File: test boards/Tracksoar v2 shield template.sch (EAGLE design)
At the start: 3 parts

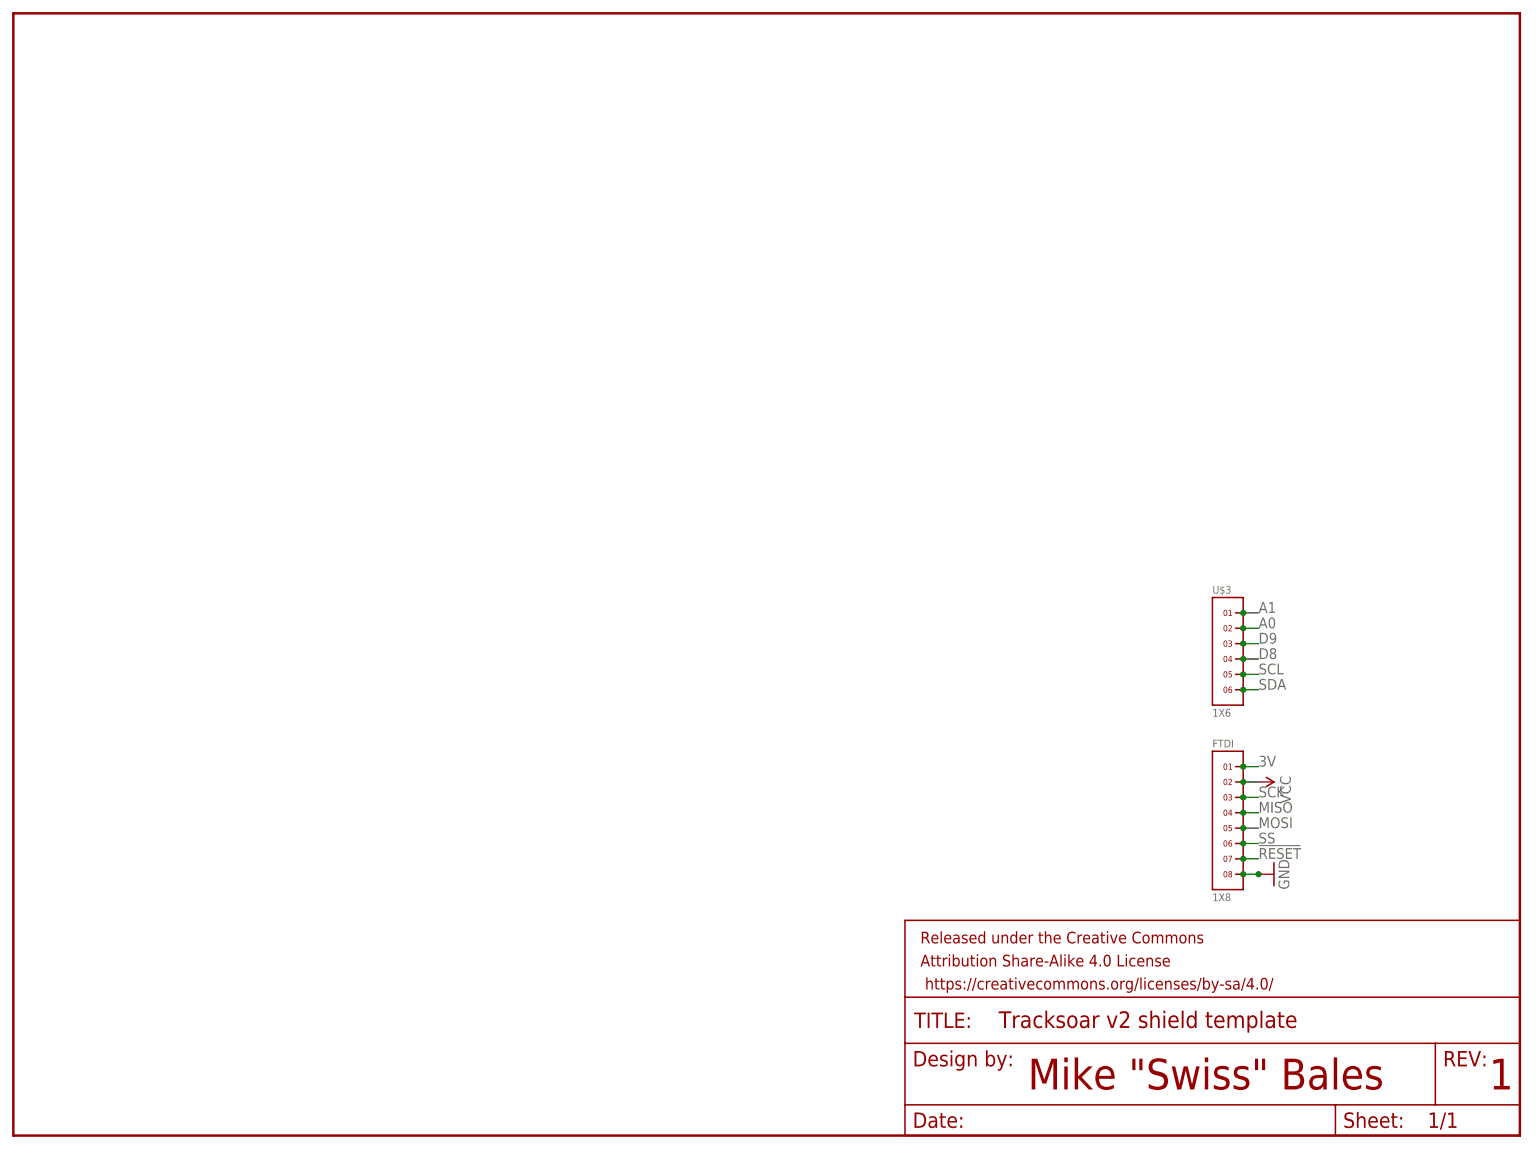
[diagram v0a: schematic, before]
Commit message: updated shield template
updated shield template to be a breakout board for all IO into .1" headers
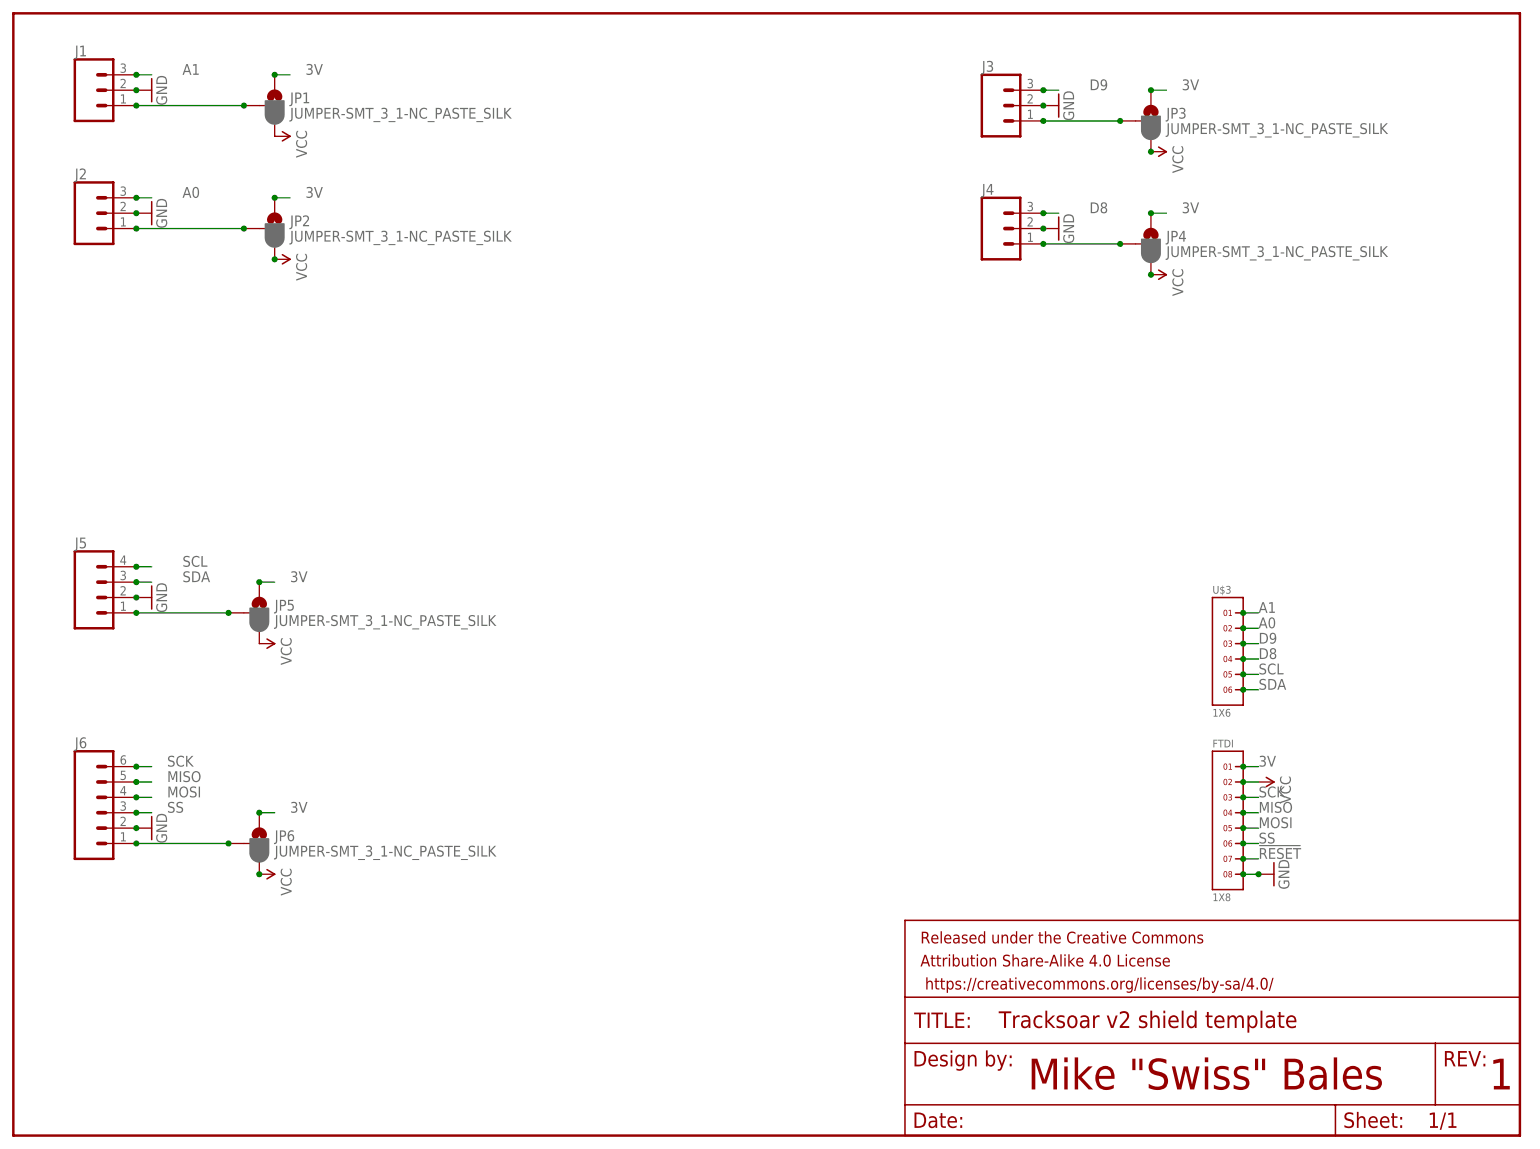
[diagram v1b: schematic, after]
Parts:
- added J1, J2, J3, J4: (no value), SparkFun-Connectors:CONN_03LONGPADS
- added J5: (no value), SparkFun-Connectors:CONN_04LONGPADS
- added J6: (no value), SparkFun-Connectors:CONN_06LONGPADS
- added JP1, JP2, JP3, JP4, JP5, JP6: JUMPER-SMT_3_1-NC_PASTE_SILK, SparkFun-Jumpers:JUMPER-SMT_3_1-NC_PASTE_SILK
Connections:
- new net N$1: J1.1, JP1.2
- new net N$2: J2.1, JP2.2
- new net N$3: J3.1, JP3.2
- new net N$6: J4.1, JP4.2
- new net N$7: J5.1, JP5.2
- new net N$8: J6.1, JP6.2
- net 3V: now also JP1.1, JP2.1, JP3.1, JP4.1, JP5.1, JP6.1
- net A0: now also J2.3
- net A1: now also J1.3
- net D8: now also J4.3
- net D9: now also J3.3
- net GND: now also J1.2, J2.2, J3.2, J4.2, J5.2, J6.2
- net MISO: now also J6.5
- net MOSI: now also J6.4
- net SCK: now also J6.6
- net SCL: now also J5.4
- net SDA: now also J5.3
- net SS: now also J6.3
- net VCC: now also JP1.3, JP2.3, JP3.3, JP4.3, JP5.3, JP6.3

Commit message: fixed short on serial RX of tracksoar v2
fixed a short on the serial rx line that shorted it to ground due to a via. Updated silkscreen on the breakout board and named headers
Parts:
- J1: value (none) -> Analog 1
- J2: value (none) -> Analog 0
- J3: value (none) -> Digital IO 9
- J4: value (none) -> Digital IO 8
- J5: value (none) -> I2C
- J6: value (none) -> SPI
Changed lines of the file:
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@@
 <?xml version="1.0" encoding="utf-8"?>
 <!DOCTYPE eagle SYSTEM "eagle.dtd">
-<eagle version="8.7.0">
+<eagle version="9.0.0">
 <drawing>
 <settings>
@@
 <part name="FTDI" library="headers(2mm)" deviceset="1X8" device=""/>
 <part name="U$3" library="headers(2mm)" deviceset="1X6" device=""/>
-<part name="J1" library="SparkFun-Connectors" library_urn="urn:adsk.eagle:library:513" deviceset="CONN_03" device="LONGPADS" package3d_urn="urn:adsk.eagle:package:38068/1"/>
-<part name="J2" library="SparkFun-Connectors" library_urn="urn:adsk.eagle:library:513" deviceset="CONN_03" device="LONGPADS" package3d_urn="urn:adsk.eagle:package:38068/1"/>
-<part name="J3" library="SparkFun-Connectors" library_urn="urn:adsk.eagle:library:513" deviceset="CONN_03" device="LONGPADS" package3d_urn="urn:adsk.eagle:package:38068/1"/>
-<part name="J4" library="SparkFun-Connectors" library_urn="urn:adsk.eagle:library:513" deviceset="CONN_03" device="LONGPADS" package3d_urn="urn:adsk.eagle:package:38068/1"/>
-<part name="J5" library="SparkFun-Connectors" library_urn="urn:adsk.eagle:library:513" deviceset="CONN_04" device="LONGPADS" package3d_urn="urn:adsk.eagle:package:38098/1"/>
-<part name="J6" library="SparkFun-Connectors" library_urn="urn:adsk.eagle:library:513" deviceset="CONN_06" device="LONGPADS" package3d_urn="urn:adsk.eagle:package:37991/1"/>
+<part name="J1" library="SparkFun-Connectors" library_urn="urn:adsk.eagle:library:513" deviceset="CONN_03" device="LONGPADS" package3d_urn="urn:adsk.eagle:package:38068/1" value="Analog 1"/>
+<part name="J2" library="SparkFun-Connectors" library_urn="urn:adsk.eagle:library:513" deviceset="CONN_03" device="LONGPADS" package3d_urn="urn:adsk.eagle:package:38068/1" value="Analog 0"/>
+<part name="J3" library="SparkFun-Connectors" library_urn="urn:adsk.eagle:library:513" deviceset="CONN_03" device="LONGPADS" package3d_urn="urn:adsk.eagle:package:38068/1" value="Digital IO 9"/>
+<part name="J4" library="SparkFun-Connectors" library_urn="urn:adsk.eagle:library:513" deviceset="CONN_03" device="LONGPADS" package3d_urn="urn:adsk.eagle:package:38068/1" value="Digital IO 8"/>
+<part name="J5" library="SparkFun-Connectors" library_urn="urn:adsk.eagle:library:513" deviceset="CONN_04" device="LONGPADS" package3d_urn="urn:adsk.eagle:package:38098/1" value="I2C"/>
+<part name="J6" library="SparkFun-Connectors" library_urn="urn:adsk.eagle:library:513" deviceset="CONN_06" device="LONGPADS" package3d_urn="urn:adsk.eagle:package:37991/1" value="SPI"/>
 <part name="JP1" library="SparkFun-Jumpers" library_urn="urn:adsk.eagle:library:528" deviceset="JUMPER-SMT_3_1-NC_PASTE" device="_SILK" package3d_urn="urn:adsk.eagle:package:39293/1"/>
 <part name="JP2" library="SparkFun-Jumpers" library_urn="urn:adsk.eagle:library:528" deviceset="JUMPER-SMT_3_1-NC_PASTE" device="_SILK" package3d_urn="urn:adsk.eagle:package:39293/1"/>

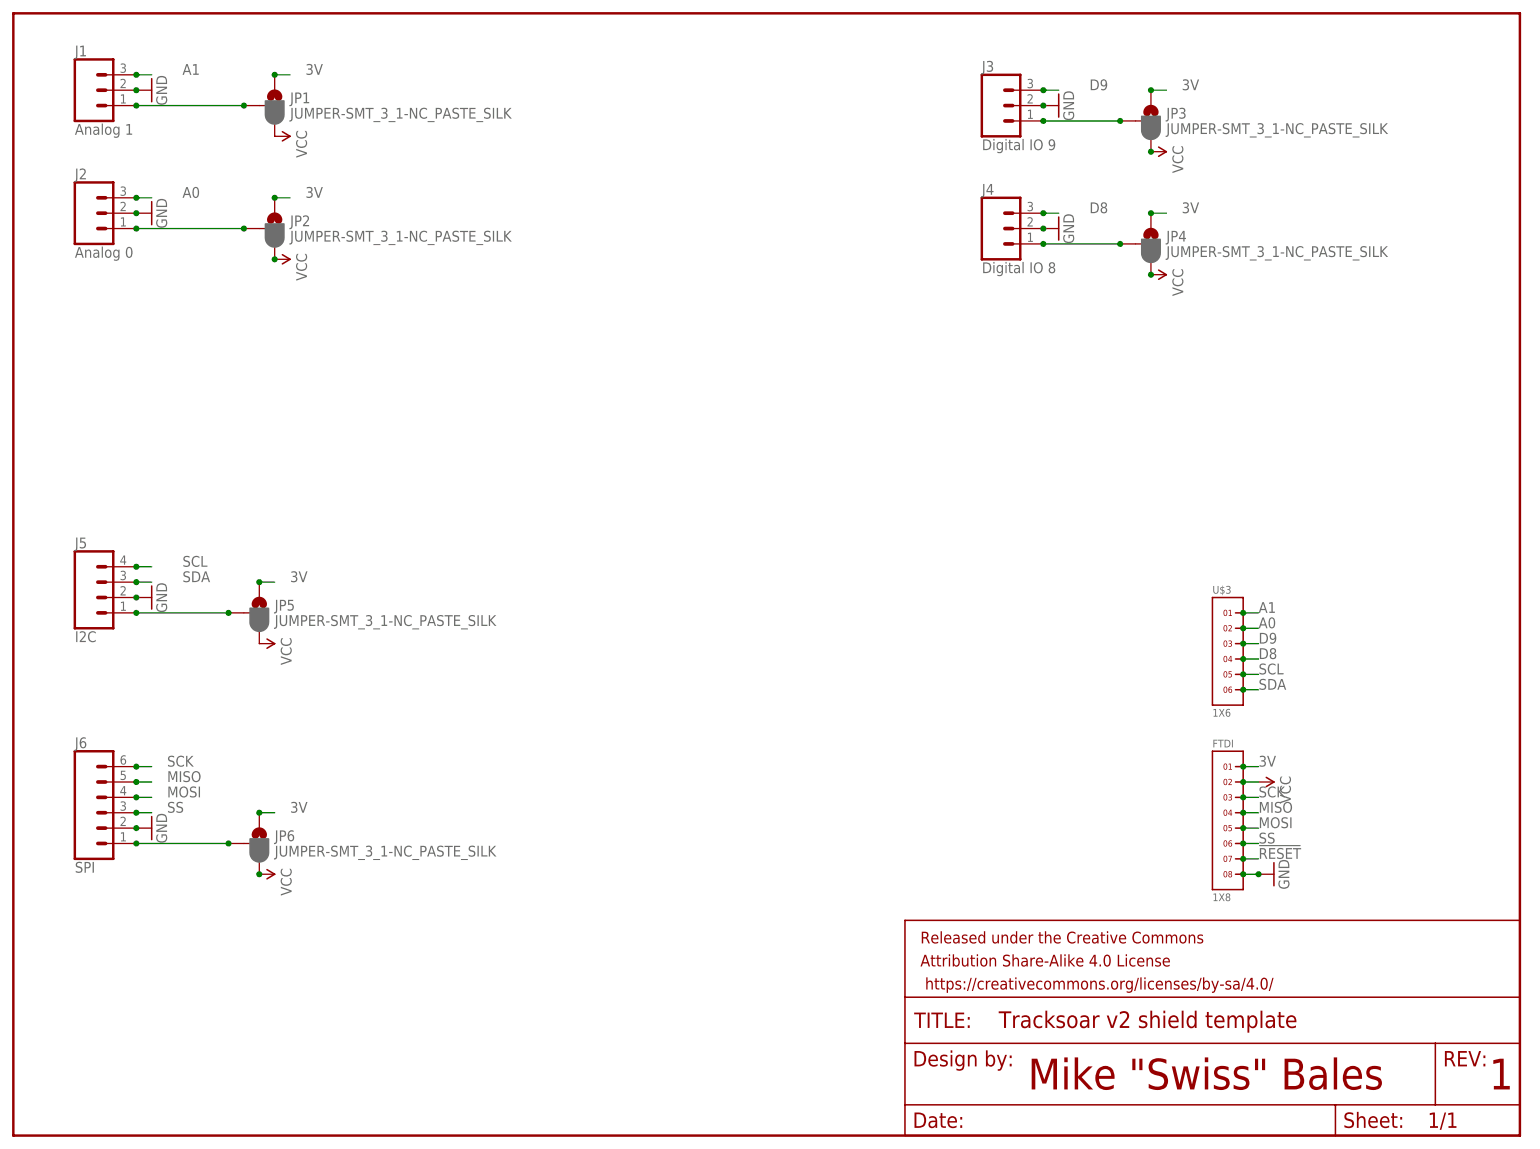
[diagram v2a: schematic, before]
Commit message: fixed the v2 shield template
renamed the breakout board and re-added the template.
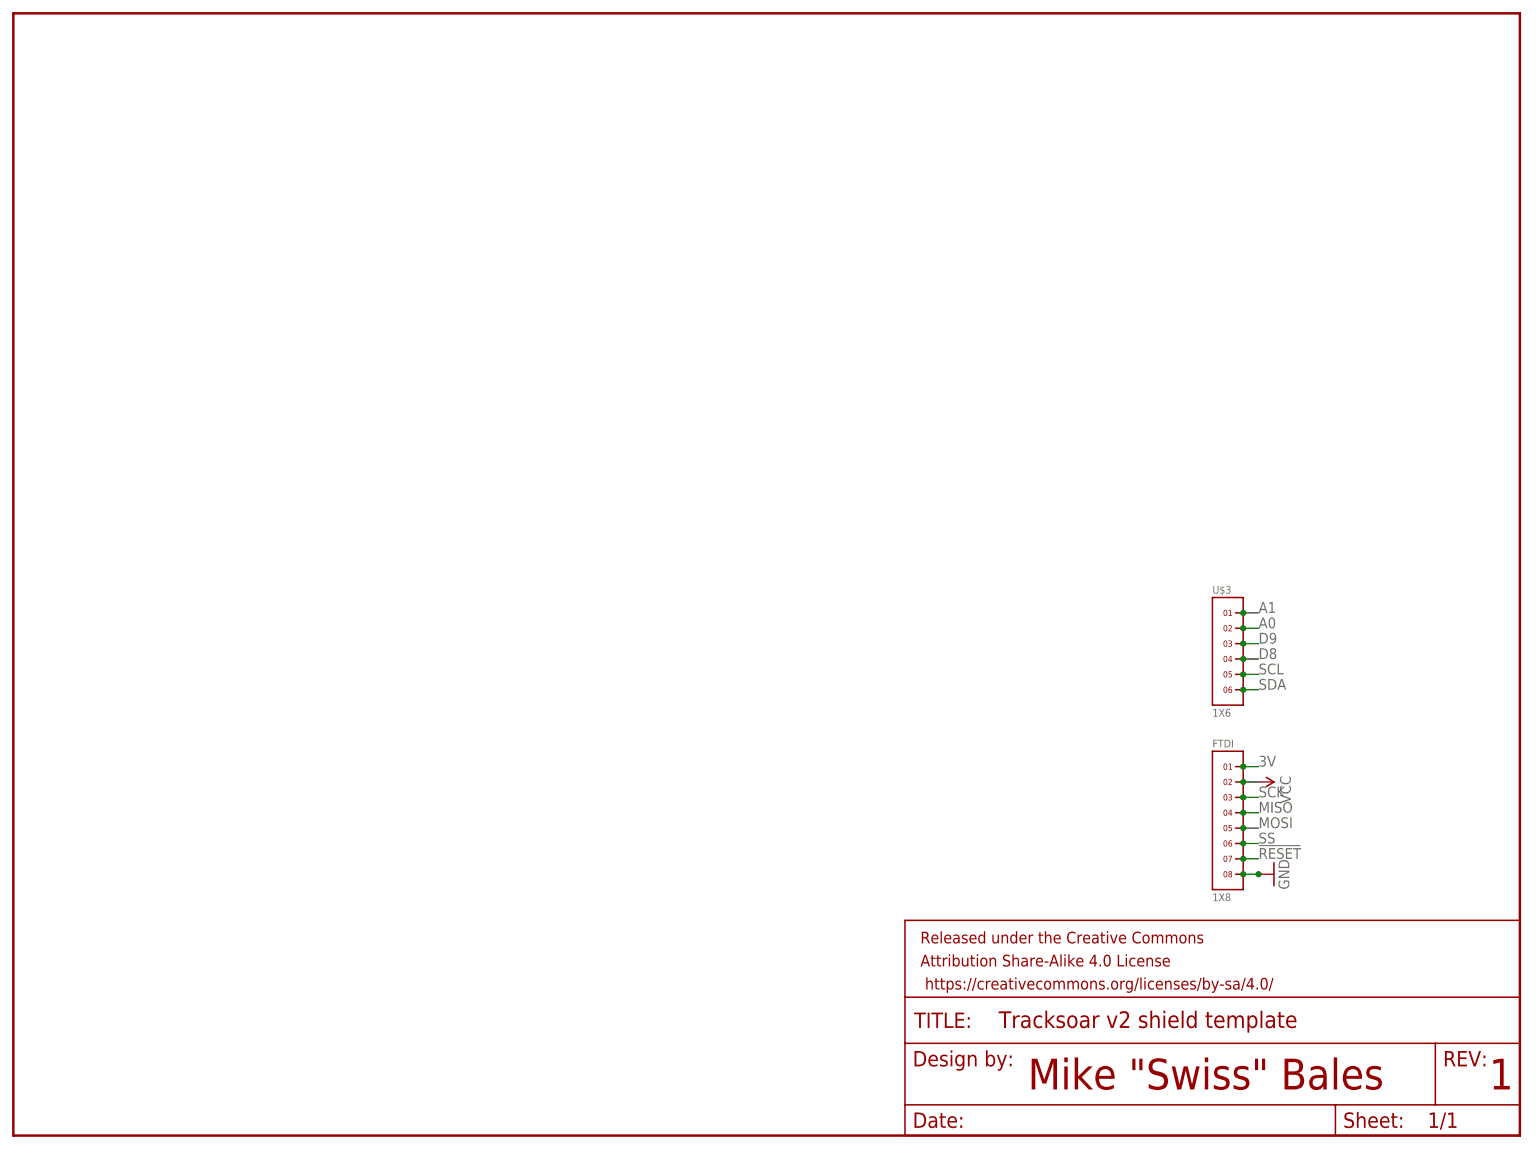
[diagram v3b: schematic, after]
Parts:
- removed J1: Analog 1, SparkFun-Connectors:CONN_03LONGPADS
- removed J2: Analog 0, SparkFun-Connectors:CONN_03LONGPADS
- removed J3: Digital IO 9, SparkFun-Connectors:CONN_03LONGPADS
- removed J4: Digital IO 8, SparkFun-Connectors:CONN_03LONGPADS
- removed J5: I2C, SparkFun-Connectors:CONN_04LONGPADS
- removed J6: SPI, SparkFun-Connectors:CONN_06LONGPADS
- removed JP1, JP2, JP3, JP4, JP5, JP6: JUMPER-SMT_3_1-NC_PASTE_SILK, SparkFun-Jumpers:JUMPER-SMT_3_1-NC_PASTE_SILK
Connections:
- removed net N$1: J1.1, JP1.2
- removed net N$2: J2.1, JP2.2
- removed net N$3: J3.1, JP3.2
- removed net N$6: J4.1, JP4.2
- removed net N$7: J5.1, JP5.2
- removed net N$8: J6.1, JP6.2
- net 3V: no longer JP1.1, JP2.1, JP3.1, JP4.1, JP5.1, JP6.1
- net A0: no longer J2.3
- net A1: no longer J1.3
- net D8: no longer J4.3
- net D9: no longer J3.3
- net GND: no longer J1.2, J2.2, J3.2, J4.2, J5.2, J6.2
- net MISO: no longer J6.5
- net MOSI: no longer J6.4
- net SCK: no longer J6.6
- net SCL: no longer J5.4
- net SDA: no longer J5.3
- net SS: no longer J6.3
- net VCC: no longer JP1.3, JP2.3, JP3.3, JP4.3, JP5.3, JP6.3
